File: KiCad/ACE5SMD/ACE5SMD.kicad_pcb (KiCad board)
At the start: 2 copper layers, 160 x 100 mm, 99 parts, among them IC1 LM7805_TO220, Q1 MMBT3904, Q3 BC847, X1 CRYSTALHC49U-V 6.556MHz, X2 5MHz

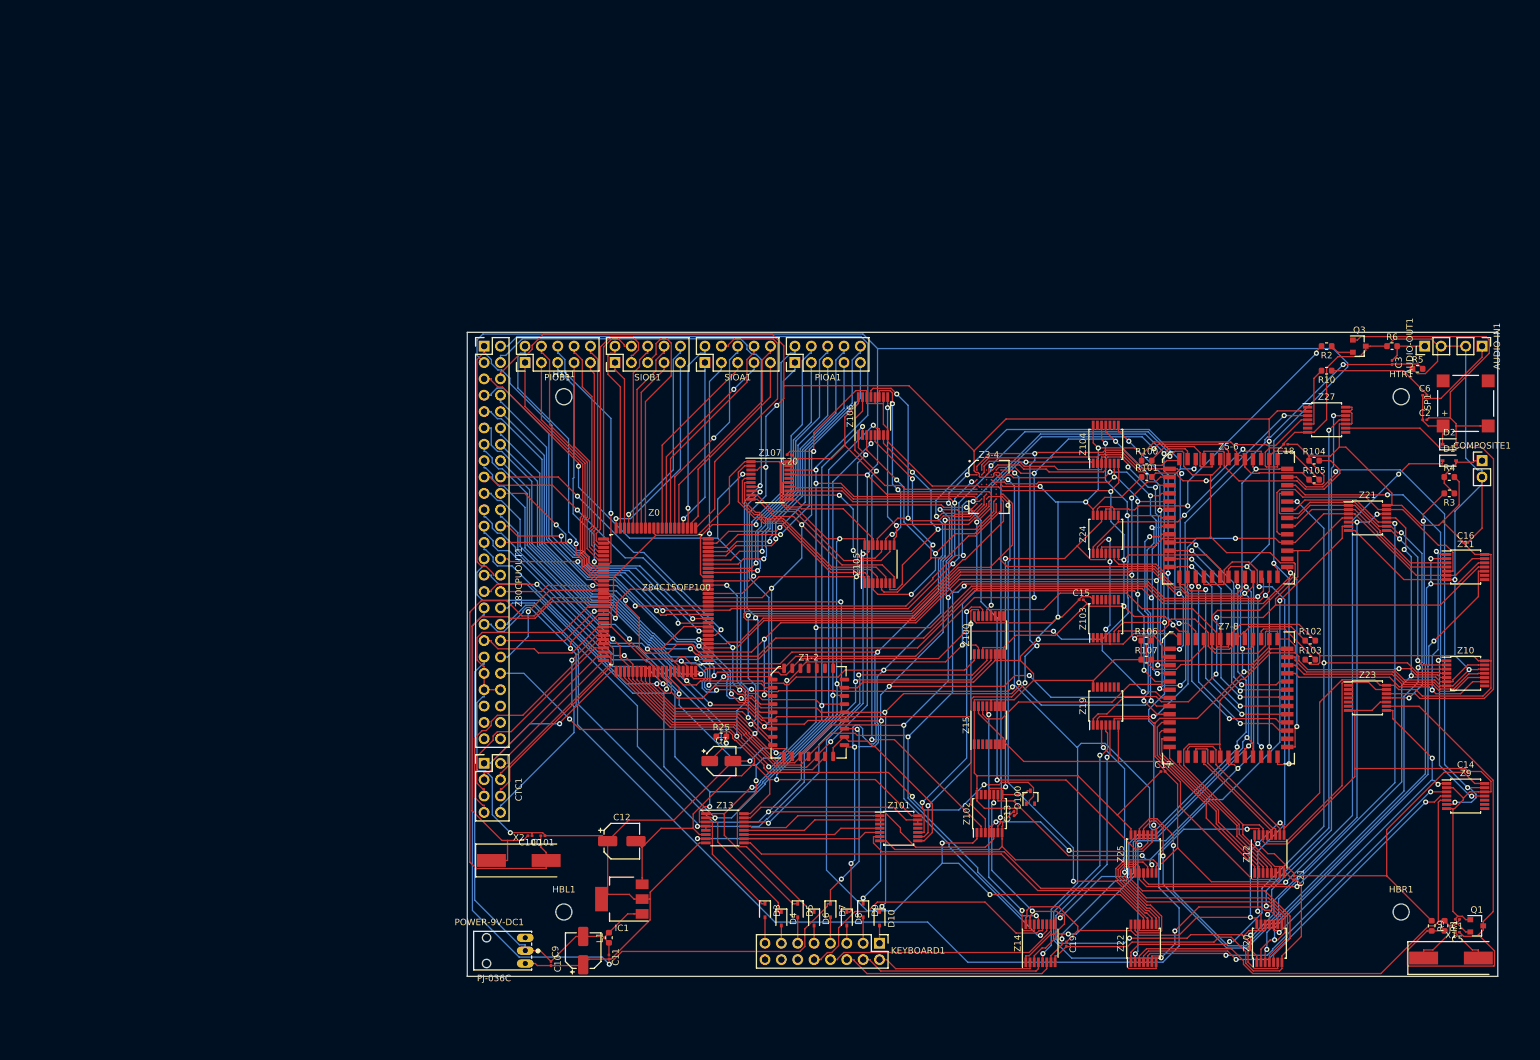
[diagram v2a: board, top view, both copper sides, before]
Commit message: Update and realign schematics. Change mount of some components.
Signed-off-by: John Bradley <flypie@rocketmail.com>
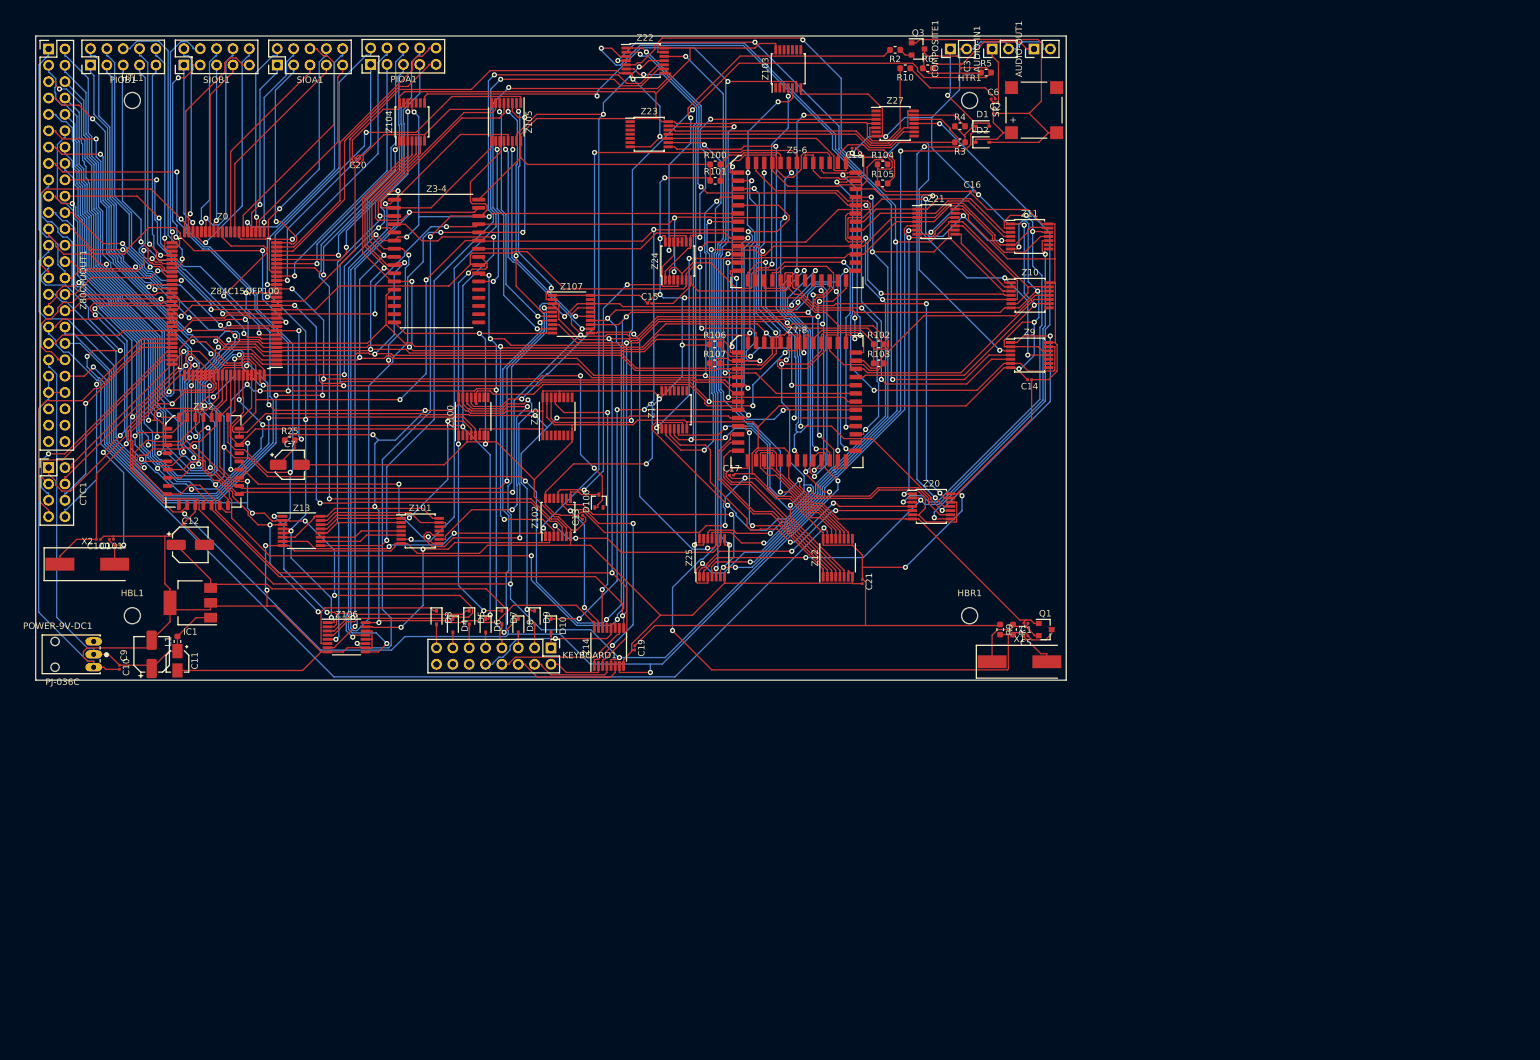
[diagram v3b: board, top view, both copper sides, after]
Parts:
- C11: value 100nf -> 100uf; footprint Capacitor_SMD:C_0201_0603Metric -> Capacitor_SMD:CP_Elec_3x5.3
- Z3-4: footprint Package_BGA:FBGA-48_6x8_6.0x8.0mm -> Package_SO:SSOP-32_11.305x20.495mm_P1.27mm
- moved Z22 157.4 mm to (94.6, 3.81), turned to 0 degrees
- moved Z23 141.8 mm to (95.2, 15.2)
- moved Z104 118.8 mm to (58.4, 13.3)
- moved COMPOSITE1 104.4 mm to (142.0, 2.00), turned to 90 degrees
- moved Z1-2 101.7 mm to (26.0, 66.0)
- moved Z103 98.6 mm to (116.8, 5.08)
- moved Z9 96.3 mm to (154.3, 49.5)
- moved C16 94.0 mm to (145.4, 24.1)
- moved R3 93.5 mm to (143.5, 16.5)
- moved R4 93.5 mm to (143.5, 14.0)
- moved Z3-4 92.7 mm to (62.2, 34.9)
- moved C14 91.0 mm to (154.3, 53.3), turned to 180 degrees
- moved Z105 89.9 mm to (73.0, 13.3), turned to 270 degrees
- moved Z10 89.6 mm to (154.4, 40.2)
- moved D1 89.2 mm to (147.0, 14.0)
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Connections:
- net Net-(COMPOSITE1-Pad1) renamed /VIDEO
- C12 pad 1: GND -> +5V
- C12 pad 2: +5V -> GND
- C9 pad 1: GND -> +9V
- C9 pad 2: +9V -> GND
- Z1-2 pad 10: /A0 -> /A1
- Z1-2 pad 11: /DA0 -> /A0
- Z1-2 pad 12: /DA1 -> Net-(Z1-2-Pad12)
- Z1-2 pad 13: /DA2 -> /DA0
- Z1-2 pad 14: GND -> /DA1
- Z1-2 pad 15: /DA3 -> /DA2
- Z1-2 pad 16: /DA4 -> GND
- Z1-2 pad 17: /DA5 -> Net-(Z1-2-Pad17)
- Z1-2 pad 18: /DA6 -> /DA3
- Z1-2 pad 19: /DA7 -> /DA4
- Z1-2 pad 2: /A12 -> Net-(Z1-2-Pad2)
- Z1-2 pad 20: Net-(Z1-2-Pad20) -> /DA5
- Z1-2 pad 21: /A10 -> /DA6
- Z1-2 pad 22: Net-(Z1-2-Pad20) -> /DA7
- Z1-2 pad 23: /A11 -> Net-(Z1-2-Pad23)
- Z1-2 pad 24: /A9 -> /A10
- Z1-2 pad 25: /A8 -> Net-(Z1-2-Pad23)
- Z1-2 pad 26: /A13 -> Net-(Z1-2-Pad26)
- Z1-2 pad 27: /A14 -> /A11
- Z1-2 pad 28: +5V -> /A9
- Z1-2 pad 29: (no net) -> /A8
- Z1-2 pad 3: /A7 -> /A12
- Z1-2 pad 30: (no net) -> /A13
- Z1-2 pad 31: (no net) -> /A14
- Z1-2 pad 32: (no net) -> +5V
- Z1-2 pad 4: /A6 -> /A7
- Z1-2 pad 5: /A5 -> /A6
- Z1-2 pad 6: /A4 -> /A5
- Z1-2 pad 7: /A3 -> /A4
- Z1-2 pad 8: /A2 -> /A3
- Z1-2 pad 9: /A1 -> /A2
- Z101 pad 8: Net-(Z1-2-Pad20) -> Net-(Z1-2-Pad23)
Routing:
- net +5V: track 848.7 -> 1009.9 mm, vias 11 -> 19
- net /DA6: track 349.8 -> 254.2 mm, vias 4 -> 9
- net #VIDEOCLK: track 52.5 -> 131.9 mm, vias 3 -> 4
- net Net-(C5-Pad1): track 78.3 -> 155.5 mm, vias 0 -> 2
- net /MA15: track 44.1 -> 118.9 mm
- net /DA7: track 310.2 -> 238.8 mm, vias 6 -> 7
- net /A11: track 244.4 -> 174.9 mm
- net /MA16: track 40.6 -> 108.1 mm
- net Net-(Z22-Pad2): track 20.5 -> 85.6 mm
- net Net-(Z22-Pad12): track 23.3 -> 87.2 mm, vias 0 -> 2
- net Net-(Z103-Pad6): track 77.6 -> 140.7 mm
- net /DA3: track 340.9 -> 280.0 mm, vias 6 -> 9
- net /MA13: track 51.3 -> 110.4 mm, vias 3 -> 4
- net /A6: track 196.1 -> 254.5 mm, vias 6 -> 8
- net Net-(Z101-Pad6): track 51.0 -> 108.4 mm, vias 0 -> 2
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
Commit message: Correct all routing.
Signed-off-by: John Bradley <flypie@rocketmail.com>
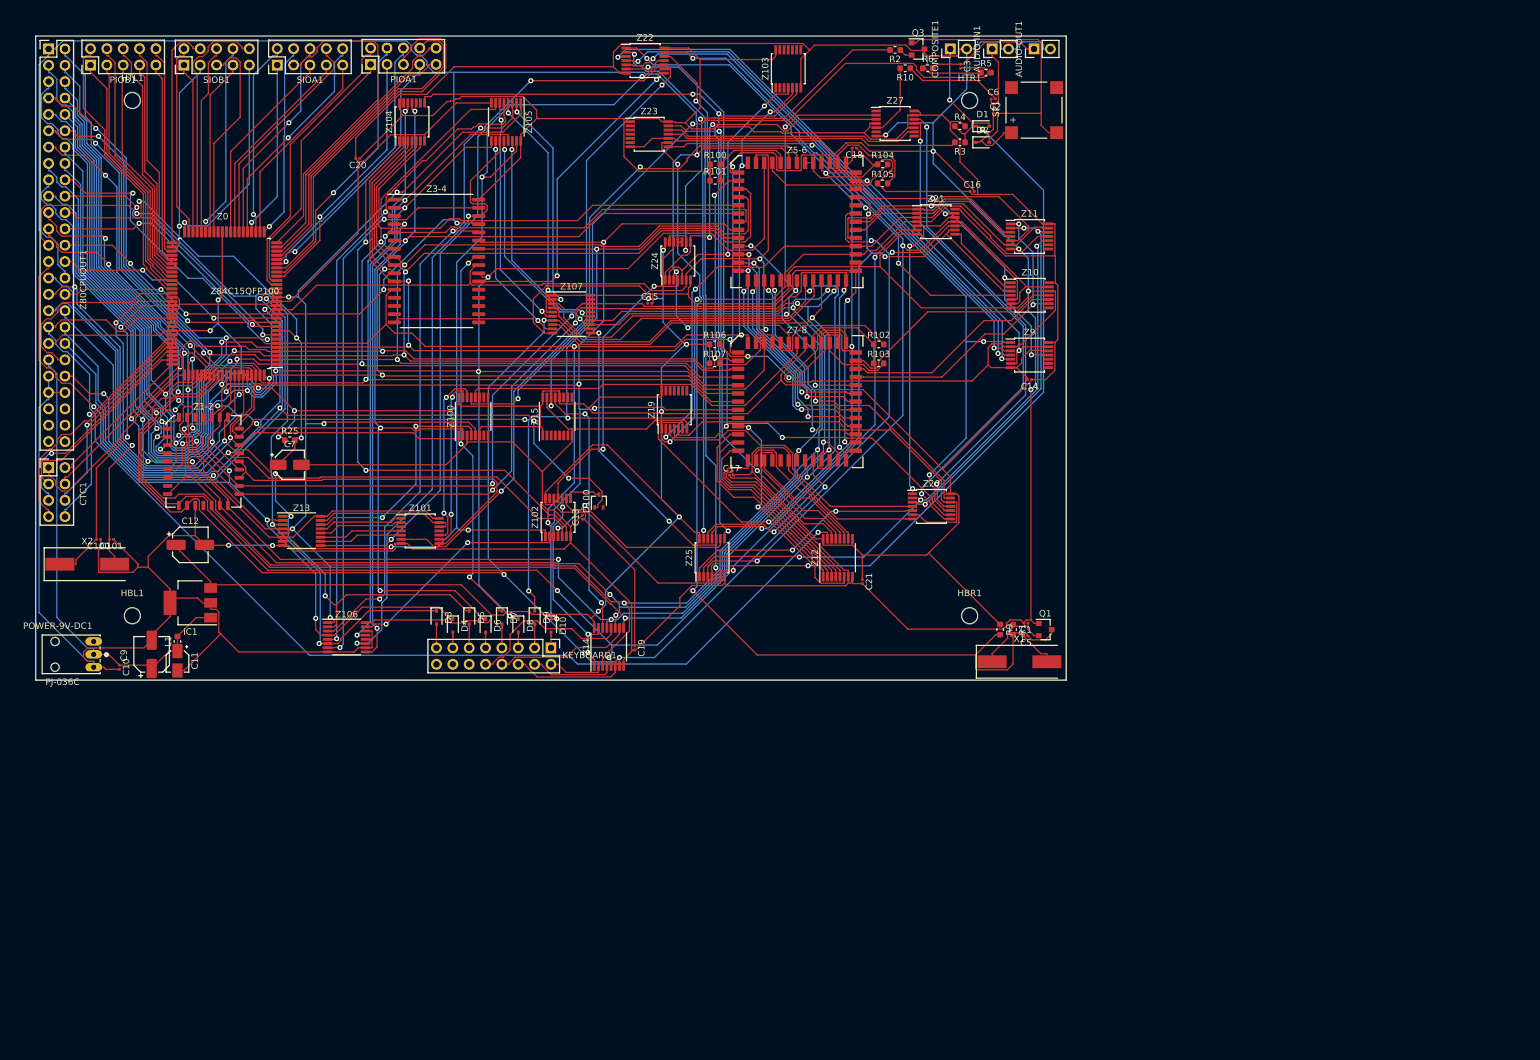
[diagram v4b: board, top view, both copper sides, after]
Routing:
- net GND: track 1009.5 -> 1116.4 mm, vias 16 -> 7
- net //WR: track 214.6 -> 279.3 mm, vias 9 -> 5
- net +5V: track 1009.9 -> 946.3 mm, vias 19 -> 12
- net /A13: track 161.3 -> 124.7 mm
- net /DA0: track 361.5 -> 325.0 mm, vias 7 -> 6
- net //RD: track 187.5 -> 153.4 mm, vias 5 -> 4
- net /A10: track 258.2 -> 292.2 mm, vias 11 -> 6
- net /A7: track 243.5 -> 276.2 mm, vias 8 -> 5
- net /A14: track 162.6 -> 131.1 mm, vias 6 -> 4
- net #VIDEOCLK: track 131.9 -> 100.8 mm, vias 4 -> 3
- net /SCREENX0: track 72.9 -> 45.8 mm
- net Net-(Z102-Pad10): track 58.4 -> 32.0 mm, vias 4 -> 3
- net /DA2: track 338.9 -> 312.8 mm, vias 7 -> 5
- net /CNT2: track 111.7 -> 86.2 mm
- net Net-(Z100-Pad14): track 53.1 -> 27.8 mm
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
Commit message: Tidy add Zilog Logo.
Signed-off-by: John Bradley <flypie@rocketmail.com>
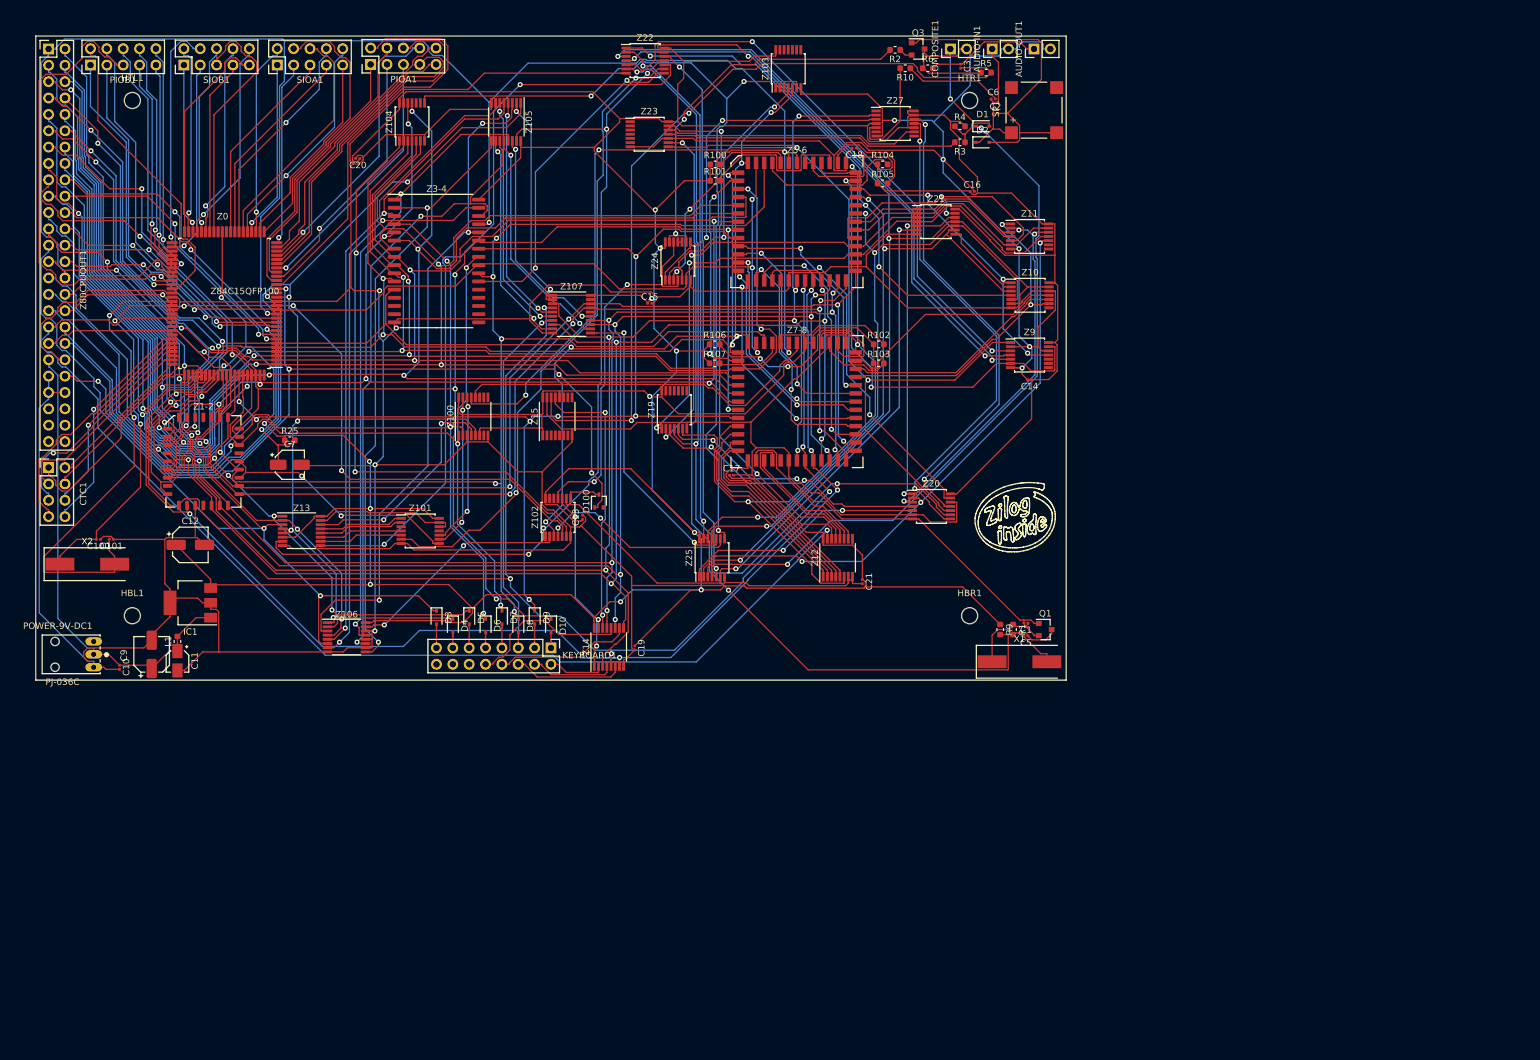
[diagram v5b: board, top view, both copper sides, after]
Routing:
- net GND: track 1116.4 -> 1024.9 mm, vias 7 -> 9
- net Net-(PIOB1-Pad5): track 35.9 -> 72.1 mm
- net /A7: track 276.2 -> 244.1 mm, vias 5 -> 7
- net //IOREQ: track 132.1 -> 105.5 mm, vias 2 -> 4
- net /SCREENX0: track 45.8 -> 70.5 mm
- net //WR: track 279.3 -> 303.9 mm, vias 5 -> 6
- net Net-(SIOA1-Pad3): track 52.6 -> 28.7 mm, vias 0 -> 1
- net Net-(C101-Pad2): track 50.6 -> 74.2 mm
- net /A3: track 267.3 -> 243.7 mm, vias 4 -> 6
- net //MREQ: track 192.7 -> 214.9 mm, vias 6 -> 5
- net +5V: track 946.3 -> 924.3 mm, vias 12 -> 14
- net /A14: track 131.1 -> 110.7 mm
- net Net-(PIOA1-Pad2): track 44.9 -> 64.2 mm
- net Net-(Z1-2-Pad23): track 57.1 -> 38.5 mm, vias 0 -> 2
- net /VIDEN: track 118.1 -> 136.3 mm
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
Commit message: Add Edge board to convert PINs to EDGECONNECTOR.
Signed-off-by: John Bradley <flypie@rocketmail.com>
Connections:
- Z3-4 pad 13: Net-(Z3-4-Pad13) -> /DA0
- Z3-4 pad 14: Net-(Z3-4-Pad14) -> /DA1
- Z3-4 pad 15: Net-(Z3-4-Pad15) -> /DA2
- Z3-4 pad 17: Net-(Z3-4-Pad17) -> /DA3
- Z3-4 pad 18: Net-(Z3-4-Pad18) -> /DA4
- Z3-4 pad 19: Net-(Z3-4-Pad19) -> /DA5
- Z3-4 pad 20: Net-(Z3-4-Pad20) -> /DA6
- Z3-4 pad 21: Net-(Z3-4-Pad21) -> /DA7
- Z80CPUOUT1 pad 1: //WR -> /#WE
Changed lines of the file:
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@@
     (zones 0)
     (modules 99)
-    (nets 276)
+    (nets 269)
   )
   (page A4)
@@
   (net 266 "Net-(Z1-2-Pad12)")
   (net 267 "Net-(Z1-2-Pad2)")
-  (net 268 "Net-(Z3-4-Pad21)")
-  (net 269 "Net-(Z3-4-Pad20)")
-  (net 270 "Net-(Z3-4-Pad19)")
-  (net 271 "Net-(Z3-4-Pad18)")
-  (net 272 "Net-(Z3-4-Pad17)")
-  (net 273 "Net-(Z3-4-Pad15)")
-  (net 274 "Net-(Z3-4-Pad14)")
-  (net 275 "Net-(Z3-4-Pad13)")
+  (net 268 /#WE)
   (net_class Default "This is the default net class."
     (clearance 0.1524)
@@
     (add_net +9V)
     (add_net /#PAGED8K)
+    (add_net /#WE)
     (add_net //BUSAK)
     (add_net //BUSRQ)
@@
     (add_net "Net-(Z27-Pad6)")
     (add_net "Net-(Z27-Pad8)")
-    (add_net "Net-(Z3-4-Pad13)")
-    (add_net "Net-(Z3-4-Pad14)")
-    (add_net "Net-(Z3-4-Pad15)")
-    (add_net "Net-(Z3-4-Pad17)")
-    (add_net "Net-(Z3-4-Pad18)")
-    (add_net "Net-(Z3-4-Pad19)")
-    (add_net "Net-(Z3-4-Pad20)")
-    (add_net "Net-(Z3-4-Pad21)")
     (add_net "Net-(Z5-6-Pad17)")
     (add_net "Net-(Z5-6-Pad18)")
@@
       (net 46 "Net-(Z22-Pad8)"))
     (pad 21 smd roundrect (at 6.55 4.445) (size 2.05 0.6) (layers Top F.Paste F.Mask) (roundrect_rratio 0.25)
-      (net 268 "Net-(Z3-4-Pad21)"))
+      (net 26 /DA7))
     (pad 20 smd roundrect (at 6.55 5.715) (size 2.05 0.6) (layers Top F.Paste F.Mask) (roundrect_rratio 0.25)
-      (net 269 "Net-(Z3-4-Pad20)"))
+      (net 28 /DA6))
     (pad 19 smd roundrect (at 6.55 6.985) (size 2.05 0.6) (layers Top F.Paste F.Mask) (roundrect_rratio 0.25)
-      (net 270 "Net-(Z3-4-Pad19)"))
+      (net 29 /DA5))
     (pad 18 smd roundrect (at 6.55 8.255) (size 2.05 0.6) (layers Top F.Paste F.Mask) (roundrect_rratio 0.25)
-      (net 271 "Net-(Z3-4-Pad18)"))
+      (net 34 /DA4))
     (pad 17 smd roundrect (at 6.55 9.525) (size 2.05 0.6) (layers Top F.Paste F.Mask) (roundrect_rratio 0.25)
-      (net 272 "Net-(Z3-4-Pad17)"))
+      (net 33 /DA3))
     (pad 16 smd roundrect (at -6.55 9.525) (size 2.05 0.6) (layers Top F.Paste F.Mask) (roundrect_rratio 0.25)
       (net 1 GND))
     (pad 15 smd roundrect (at -6.55 8.255) (size 2.05 0.6) (layers Top F.Paste F.Mask) (roundrect_rratio 0.25)
-      (net 273 "Net-(Z3-4-Pad15)"))
+      (net 27 /DA2))
     (pad 14 smd roundrect (at -6.55 6.985) (size 2.05 0.6) (layers Top F.Paste F.Mask) (roundrect_rratio 0.25)
-      (net 274 "Net-(Z3-4-Pad14)"))
+      (net 24 /DA1))
     (pad 13 smd roundrect (at -6.55 5.715) (size 2.05 0.6) (layers Top F.Paste F.Mask) (roundrect_rratio 0.25)
-      (net 275 "Net-(Z3-4-Pad13)"))
+      (net 25 /DA0))
     (pad 12 smd roundrect (at -6.55 4.445) (size 2.05 0.6) (layers Top F.Paste F.Mask) (roundrect_rratio 0.25)
       (net 12 /A0))
@@
       (net 26 /DA7))
     (pad 1 thru_hole rect (at 0 0) (size 1.7 1.7) (drill 1) (layers *.Cu *.Mask)
-      (net 18 //WR))
+      (net 268 /#WE))
     (model ${KISYS3DMOD}/Connector_PinHeader_2.54mm.3dshapes/PinHeader_2x25_P2.54mm_Vertical.wrl
       (at (xyz 0 0 0))

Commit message: Improve consitancy.
Signed-off-by: John Bradley <flypie@rocketmail.com>
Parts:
- added R32: 1K0, Resistor_THT:R_Axial_DIN0204_L3.6mm_D1.6mm_P2.54mm_Vertical, F.Cu at (31.5, 15.2)
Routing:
- net //WR: track 303.9 -> 177.9 mm, vias 6 -> 5
- net /DA2: track 303.5 -> 384.2 mm, vias 7 -> 6
- net +5V: track 924.3 -> 849.7 mm, vias 14 -> 16
- net Net-(R32-Pad2): track 51.2 -> 115.2 mm
- net //IOREQ: track 105.5 -> 154.6 mm, vias 4 -> 2
- net /DA7: track 230.0 -> 274.9 mm
- net //INT: track 135.2 -> 177.3 mm, vias 5 -> 3
- net GND: track 1024.9 -> 1066.4 mm
- net //RD: track 149.5 -> 187.3 mm, vias 5 -> 4
- net Net-(PIOB1-Pad5): track 72.1 -> 35.8 mm, vias 0 -> 1
- net /A10: track 280.7 -> 316.4 mm
- net /DA0: track 330.6 -> 295.1 mm, vias 7 -> 8
- net /#WE: track 0.00 -> 35.1 mm
- net /SCREENX2: track 98.0 -> 132.3 mm
- net /A5: track 255.9 -> 289.1 mm, vias 4 -> 5
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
